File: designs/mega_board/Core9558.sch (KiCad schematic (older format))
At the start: 0 parts

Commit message: Almost finish the main schematic with connectors and block interconnection
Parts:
- added U?: Core9558, MODULE, symbol LibreRouter_MegaBoard-rescue:Core9558-Core9558
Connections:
- new net COM_A_2G: U?.2 (COM_A_2G)
- new net COM_B_2G: U?.3 (COM_B_2G)
- new net GPIO0-EJTAG_TCK: U?.7 (EJTAG_TCK/GPIO0)
- new net GPIO1-EJTAG_TDI: U?.8 (EJTAG_TDI/GPIO1)
- new net GPIO12: U?.20 (GPIO12)
- new net GPIO13: U?.21 (GPIO13)
- new net GPIO14: U?.22 (GPIO14)
- new net GPIO15: U?.23 (GPIO15)
- new net GPIO16: U?.24 (GPIO16)
- new net GPIO17: U?.25 (GPIO17)
- new net GPIO18: U?.26 (GPIO18)
- new net GPIO19: U?.27 (GPIO19)
- new net GPIO2-EJTAG_TDO: U?.9 (EJTAG_TDO/GPIO2)
- new net GPIO20: U?.28 (GPIO20)
- new net GPIO21: U?.29 (GPIO21)
- new net GPIO22: U?.30 (GPIO22)
- new net GPIO23: U?.31 (GPIO23)
- new net GPIO3-EJTAG_TMS: U?.10 (EJTAG_TMS/GPIO3)
- new net GPIO4: U?.17 (GPIO4)
- new net PCIE0_CLK_N_CONN: U?.124 (PCIE0_CLK_N_CONN)
- new net PCIE0_CLK_P_CONN: U?.125 (PCIE0_CLK_P_CONN)
- new net PCIE0_RST_L: U?.123 (PCIE0_RST_L)
- new net PCIE0_RX_N_CONN: U?.127 (PCIE0_RX_N_CONN)
- new net PCIE0_RX_P_CONN: U?.128 (PCIE0_RX_P_CONN)
- new net PCIE0_TX_N_CONN: U?.130 (PCIE0_TX_N_CONN)
- new net PCIE0_TX_P_CONN: U?.131 (PCIE0_TX_P_CONN)
- new net PCIE1_CLK_N_CONN: U?.121 (PCIE1_CLK_N_CONN)
- new net PCIE1_CLK_P_CONN: U?.120 (PCIE1_CLK_P_CONN)
- new net PCIE1_RST_L: U?.122 (PCIE1_RST_L)
- new net PCIE1_RX_N_CONN: U?.118 (PCIE1_RX_N_CONN)
- new net PCIE1_RX_P_CONN: U?.117 (PCIE1_RX_P_CONN)
- new net PCIE1_TX_N_CONN: U?.115 (PCIE1_TX_N_CONN)
- new net PCIE1_TX_P_CONN: U?.114 (PCIE1_TX_P_CONN)
- new net RST_B: U?.6 (RST_B)
- new net S17_LEDN1000_3: U?.106 (S17_LEDN1000_3)
- new net S17_LEDN1000_4: U?.108 (S17_LEDN1000_4)
- new net S17_LEDN_3: U?.105 (S17_LEDN_3)
- new net S17_LEDN_4: U?.107 (S17_LEDN_4)
- new net S17_P3_TRX0+: U?.76 (S17_P3_TRX0+)
- new net S17_P3_TRX0-: U?.77 (S17_P3_TRX0-)
- new net S17_P3_TRX1+: U?.78 (S17_P3_TRX1+)
- new net S17_P3_TRX1-: U?.79 (S17_P3_TRX1-)
- new net S17_P3_TRX2+: U?.80 (S17_P3_TRX2+)
- new net S17_P3_TRX2-: U?.81 (S17_P3_TRX2-)
- new net S17_P3_TRX3+: U?.82 (S17_P3_TRX3+)
- new net S17_P3_TRX3-: U?.83 (S17_P3_TRX3-)
- new net S17_P4_TRX0+: U?.85 (S17_P4_TRX0+)
- new net S17_P4_TRX0-: U?.86 (S17_P4_TRX0-)
- new net S17_P4_TRX1+: U?.87 (S17_P4_TRX1+)
- new net S17_P4_TRX1-: U?.88 (S17_P4_TRX1-)
- new net S17_P4_TRX2+: U?.89 (S17_P4_TRX2+)
- new net S17_P4_TRX2-: U?.90 (S17_P4_TRX2-)
- new net S17_P4_TRX3+: U?.91 (S17_P4_TRX3+)
- new net S17_P4_TRX3-: U?.92 (S17_P4_TRX3-)
- new net SPI_CLK: U?.110 (SPI_CLK)
- new net SPI_CS_L: U?.109 (SPI_CS_L)
- new net SPI_MISO: U?.112 (SPI_MISO)
- new net SPI_MOSI: U?.111 (SPI_MOSI)
- new net UART_SIN: U?.18 (UART_SIN)
- new net UART_SOUT: U?.19 (UART_SOUT)
- new net USB0_DM: U?.34 (USB2_DM)
- new net USB0_DP: U?.33 (USB2_DP)
- new net USB1_DM: U?.37 (USB1_DM)
- new net USB1_DP: U?.36 (USB1_DP)
- no-connect marks 0 -> 30

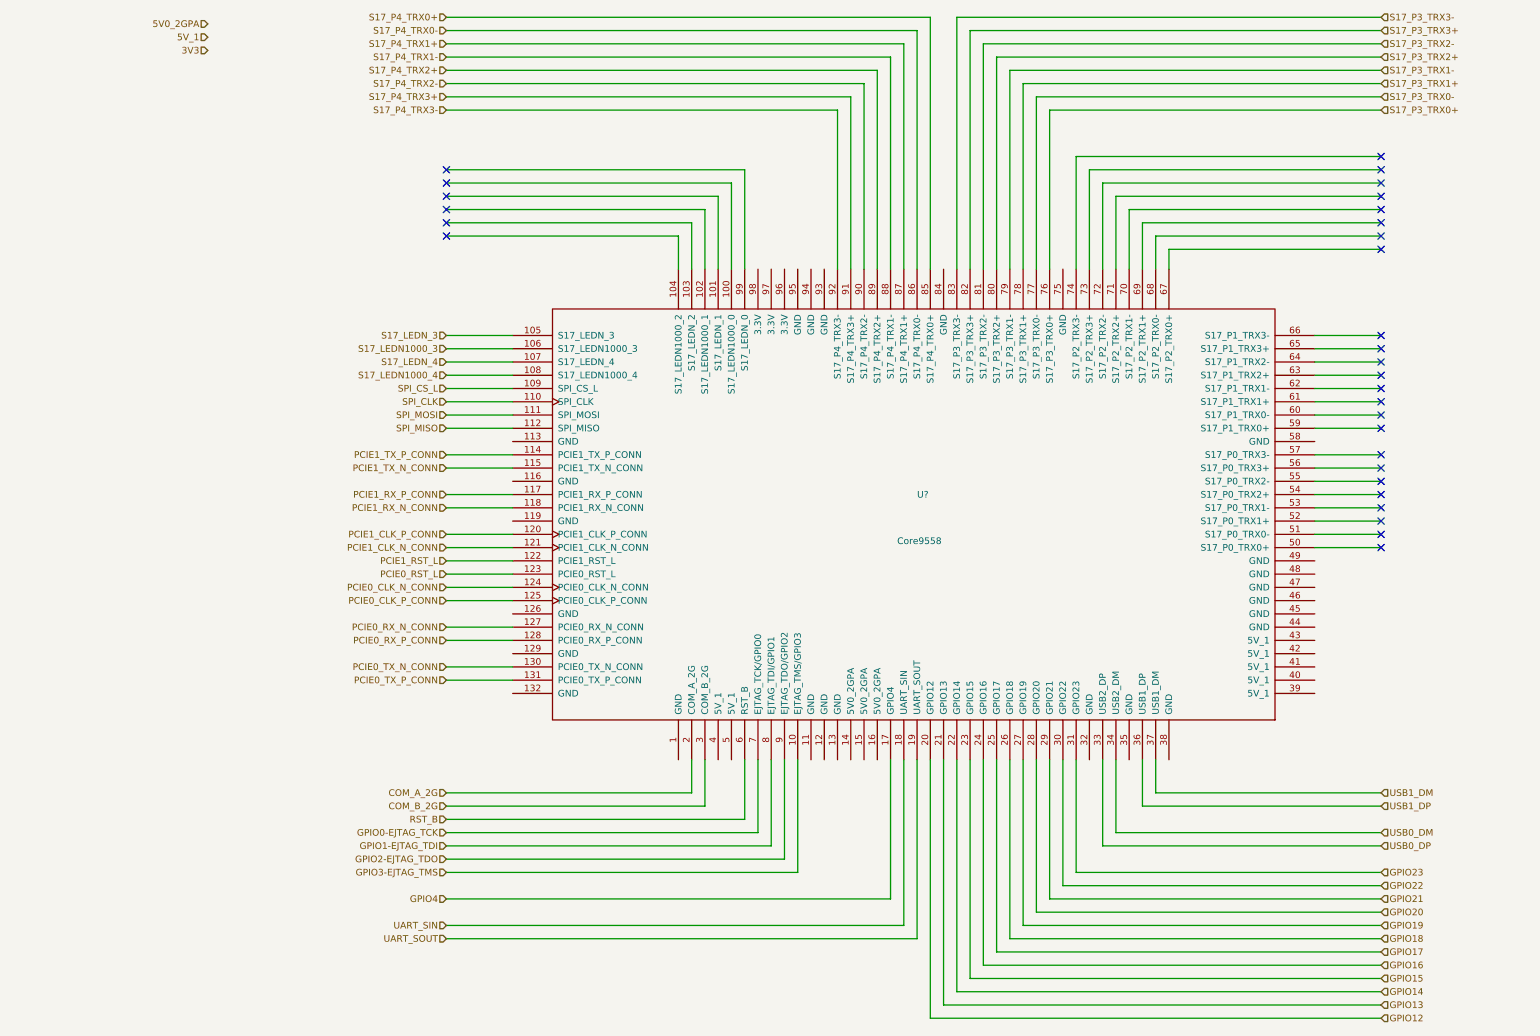
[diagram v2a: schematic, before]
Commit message: Add power connections to core
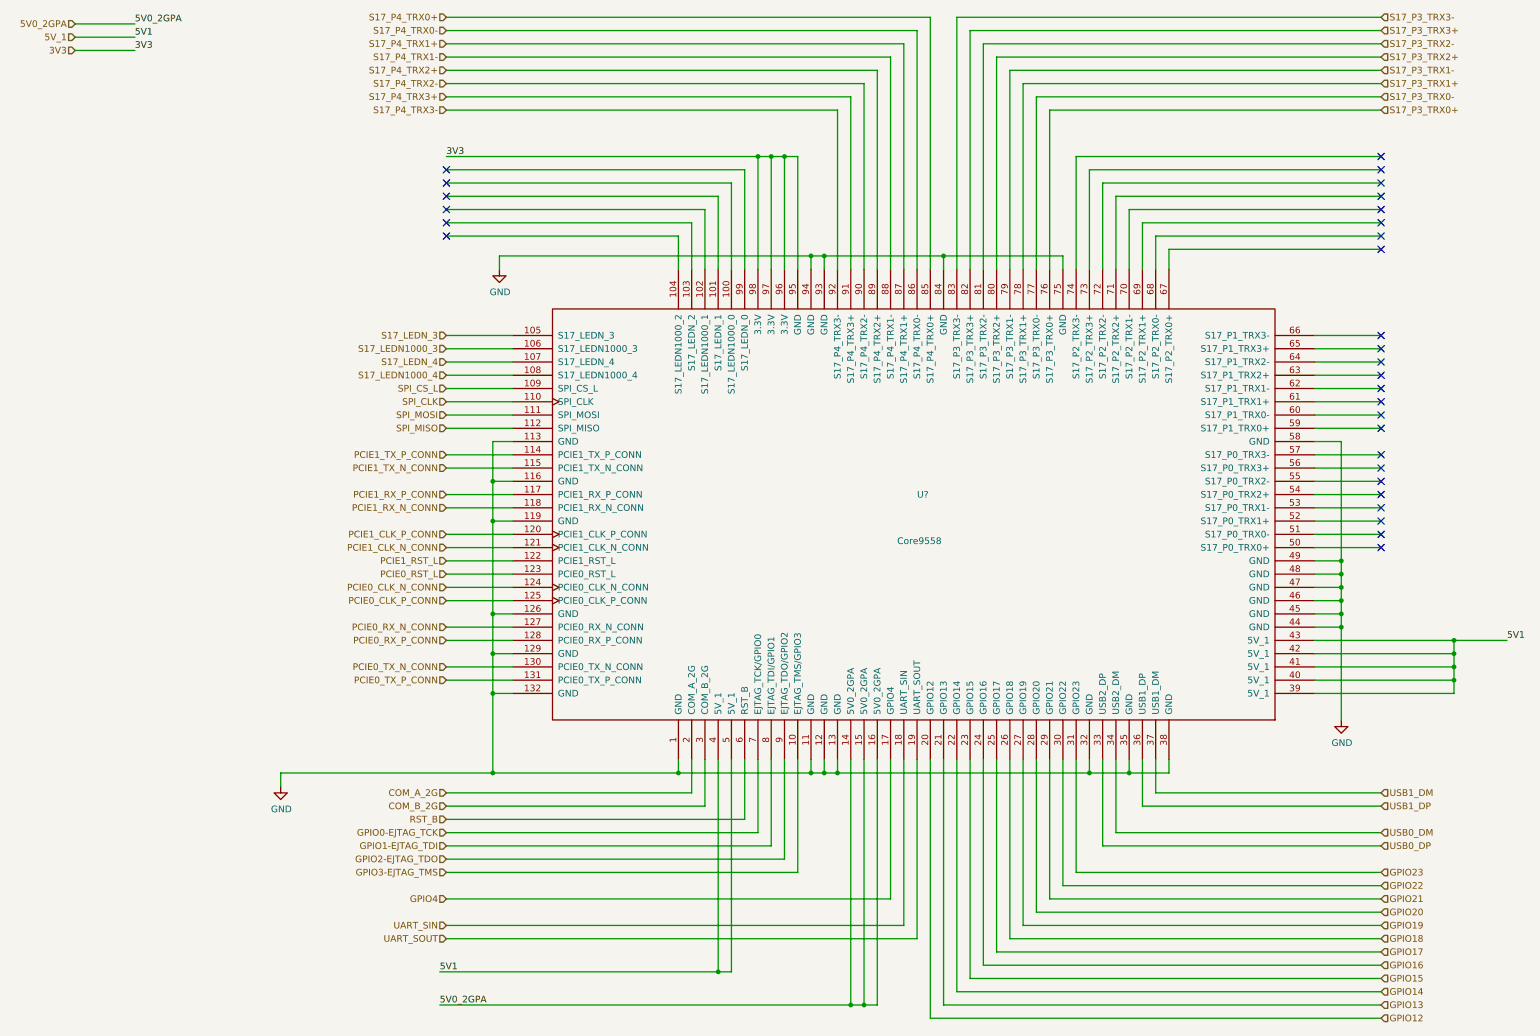
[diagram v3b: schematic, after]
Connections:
- net 3V3: now also U?.95 (GND), U?.96 (3.3V), U?.97 (3.3V), U?.98 (3.3V)
- net 5V0_2GPA: now also U?.14 (5V0_2GPA), U?.15 (5V0_2GPA), U?.16 (5V0_2GPA)
- net 5V_1: now also U?.39 (5V_1), U?.4 (5V_1), U?.40 (5V_1), U?.41 (5V_1), U?.42 (5V_1), U?.43 (5V_1), U?.5 (5V_1)
- net GND: now reaches U?.1 (GND)
- net GND: now also U?.11 (GND), U?.113 (GND), U?.116 (GND), U?.119 (GND), U?.12 (GND), U?.126 (GND), U?.129 (GND), U?.13 (GND), U?.132 (GND), U?.32 (GND), U?.35 (GND), U?.38 (GND), U?.44 (GND), U?.45 (GND), U?.46 (GND), U?.47 (GND), U?.48 (GND), U?.49 (GND), U?.58 (GND), U?.75 (GND), U?.84 (GND), U?.93 (GND), U?.94 (GND)
